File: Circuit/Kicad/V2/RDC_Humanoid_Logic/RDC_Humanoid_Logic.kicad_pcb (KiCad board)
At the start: 2 copper layers, 157 x 137 mm, 70 parts, among them J1 XT30, J2 Conn_01x03, J3 Conn_01x03, J4 Raspi_connect, Q1 Q_PMOS_GDS, Q2 Q_PMOS_GDS, SW1 SW_SPDT, SW2 SW_SPDT, SW3 SW_SPDT, U1 ISOW1044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

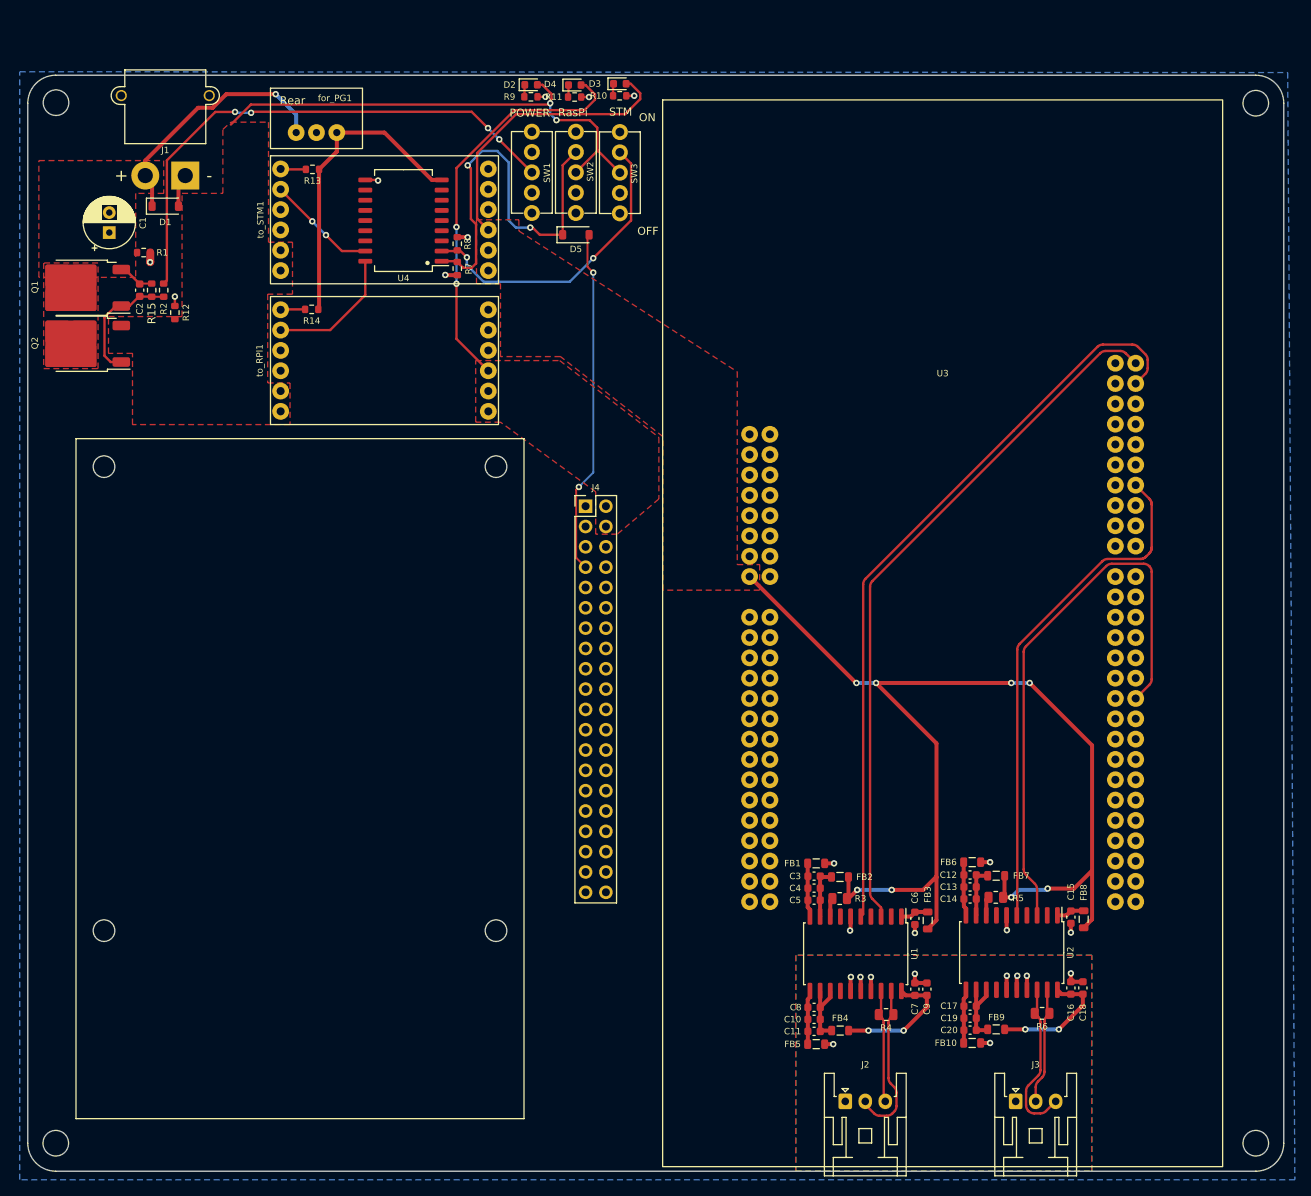
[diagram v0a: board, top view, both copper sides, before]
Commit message: V2をUpdate。FrontをベタGND、CANトランシーバのSTANDBYとINをGNDに接続、ビアを複数配置、XT30->XT60に更新、D1を回路図通りショットキーバリアダイオードに変更した。
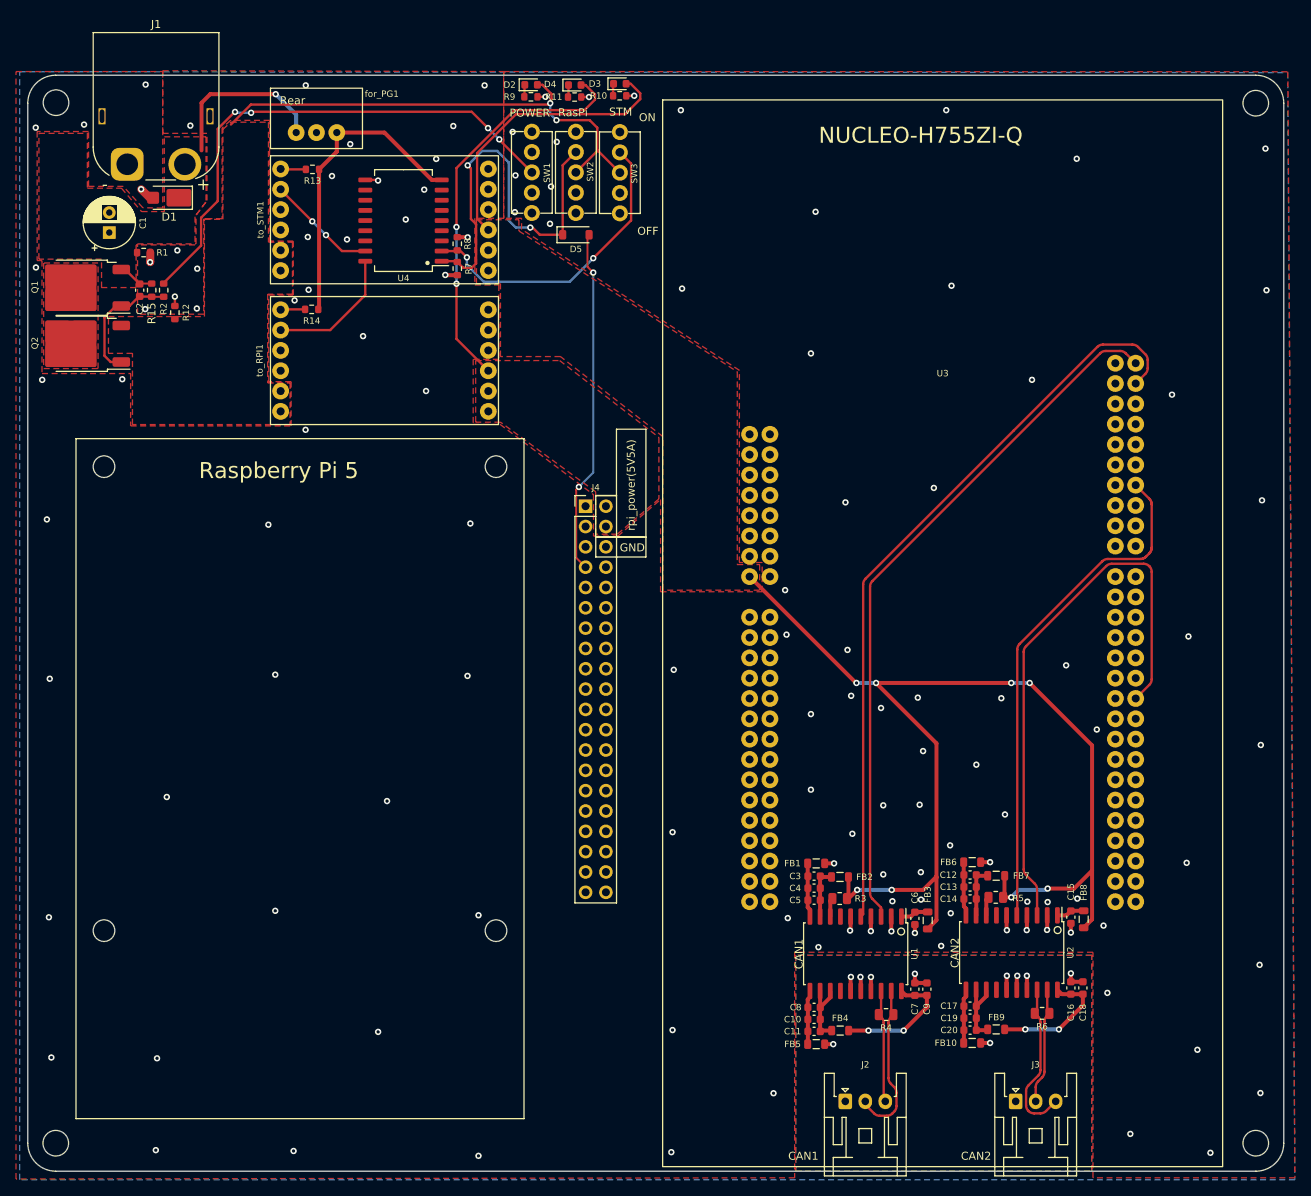
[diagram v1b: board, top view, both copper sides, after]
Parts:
- D1: value D -> D_Schottky; footprint Diode_SMD:D_SOD-123 -> Diode_SMD:Vishay_SMPA
- J1: value XT30 -> XT60; footprint Connector_AMASS:AMASS_XT30PW-M_1x02_P2.50mm_Horizontal -> Connector_AMASS:AMASS_XT60PW-M_1x02_P7.20mm_Horizontal
- moved J1 7.39 mm to (79.9, 35.5)
- moved D1 1.16 mm to (85.2, 39.6), turned to 180 degrees
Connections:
- U1 pad 2: /CAN_Trans1/GPIO -> GND
- U1 pad 4: /CAN_Trans1/STANBY -> GND
- U2 pad 2: /CAN_Trans2/GPIO -> GND
- U2 pad 4: /CAN_Trans2/STANBY -> GND
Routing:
- net +12V: track 36.2 -> 26.1 mm
- net GND: track 22.2 -> 27.3 mm, vias 14 -> 126
- net Net-(SW1-B): track 67.0 -> 65.5 mm
- added copper zone on F.Cu, net GND
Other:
- board text added: "CAN1"
- board text added: "CAN2"
- board text added: "GND"
- board text added: "NUCLEO-H755ZI-Q"
- board text added: "RDC_Bipedal_Robot - Circuit Name : Logic_Board - Version : 2.0 - Update Date : 2025/03/11 - Author Name - Main : Yuya Mochizuki - Sub : Yusuke Yamasaki"
- board text added: "Raspberry Pi 5"
- board text added: "rpi_power(5V5A)"

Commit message: V2基板手直し
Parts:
- moved R12 0.10 mm to (86.0, 54.0)
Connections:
- C10 pad 2: GND3 -> Net-(U1-GND2)
- C11 pad 2: GND3 -> Net-(U1-GND2)
- C12 pad 2: GND2 -> Net-(U2-GND1)
- C13 pad 2: GND2 -> Net-(U2-GND1)
- C14 pad 2: GND2 -> Net-(U2-GND1)
- C17 pad 2: GND3 -> Net-(U2-GND2)
- C19 pad 2: GND3 -> Net-(U2-GND2)
- C20 pad 2: GND3 -> Net-(U2-GND2)
- C3 pad 2: GND2 -> Net-(U1-GND1)
- C4 pad 2: GND2 -> Net-(U1-GND1)
- C5 pad 2: GND2 -> Net-(U1-GND1)
- C8 pad 2: GND3 -> Net-(U1-GND2)
- FB1 pad 2: GND2 -> Net-(U1-GND1)
- FB10 pad 1: GND3 -> Net-(U2-GND2)
- FB5 pad 1: GND3 -> Net-(U1-GND2)
- FB6 pad 2: GND2 -> Net-(U2-GND1)
- U1 pad 10: GND2 -> Net-(U1-GND1)
- U1 pad 11: GND3 -> Net-(U1-GND2)
- U2 pad 10: GND2 -> Net-(U2-GND1)
- U2 pad 11: GND3 -> Net-(U2-GND2)
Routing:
- net GND3: track 13.6 -> 0.00 mm
- net GND2: track 13.5 -> 0.00 mm
- net Net-(U2-GND2): track 0.00 -> 6.79 mm
- net Net-(U1-GND2): track 0.00 -> 6.79 mm
- net Net-(U1-GND1): track 0.00 -> 6.77 mm
- net Net-(U2-GND1): track 0.00 -> 6.77 mm
- net GND: vias 126 -> 128
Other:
- board text added: "RDC_Bipedal_Robot - Circuit Name : Logic_Board - Version : 2.0 - Designed Date : 2025/03/11 - Designer Name - Yuya Mochizuki - Yusuke Yamasaki"
- board text removed: "RDC_Bipedal_Robot - Circuit Name : Logic_Board - Version : 2.0 - Update Date : 2025/03/11 - Author Name - Main : Yuya Mochizuki - Sub : Yusuke Yamasaki"

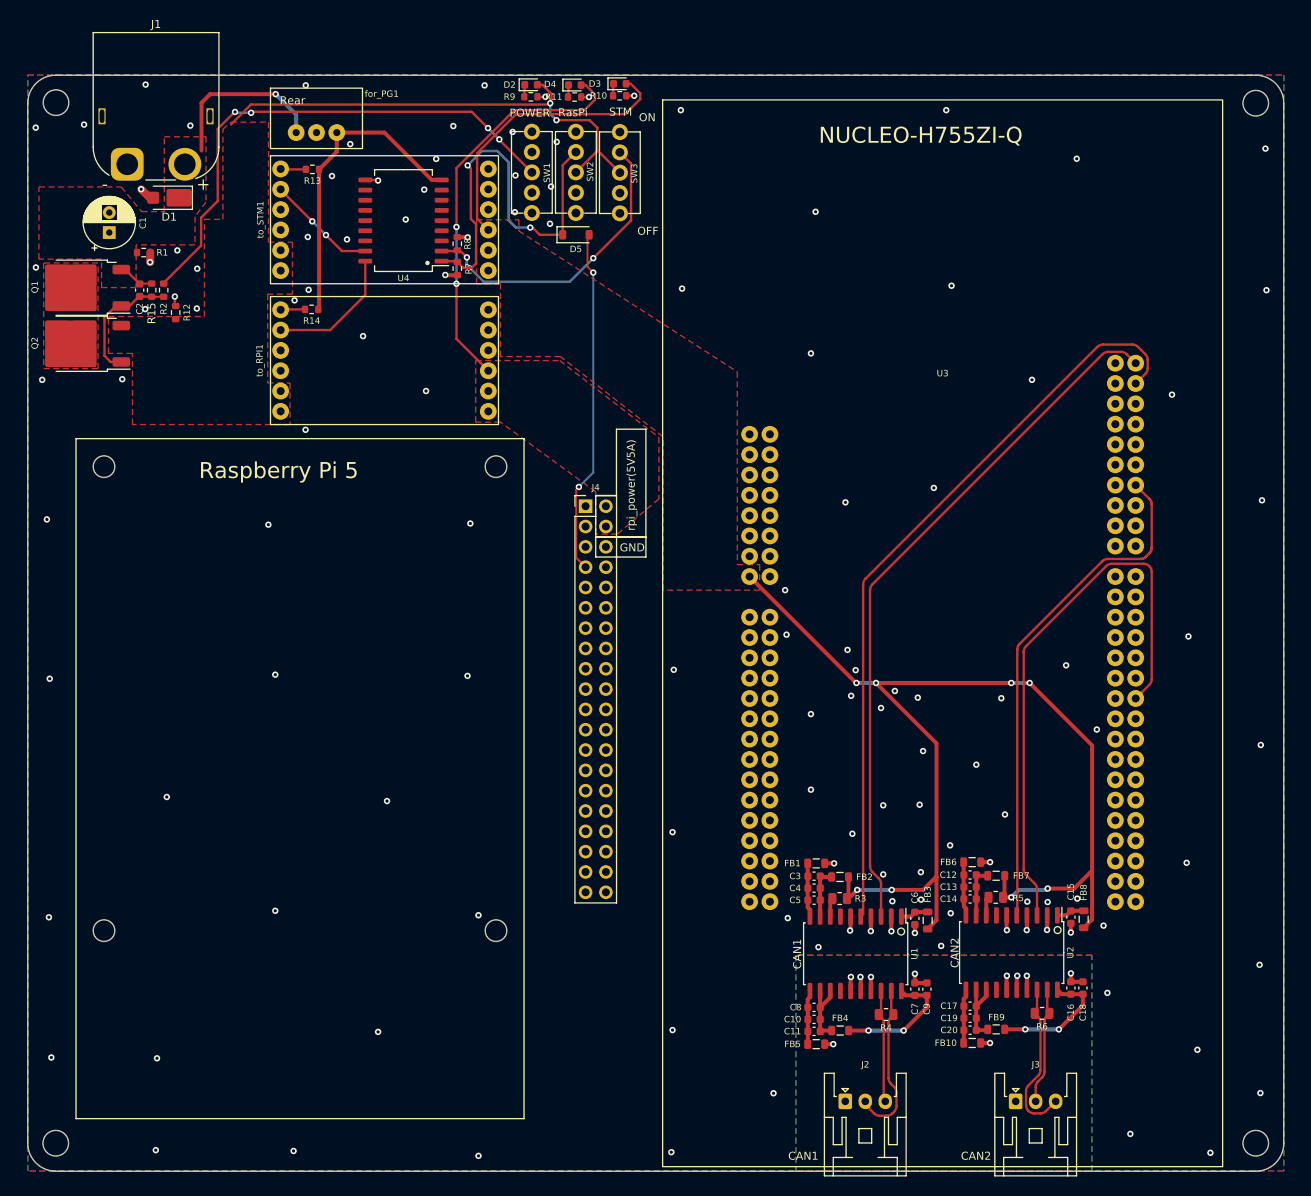
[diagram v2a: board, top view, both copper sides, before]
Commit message: ビアを増やした。おおよそV2は良いだろう
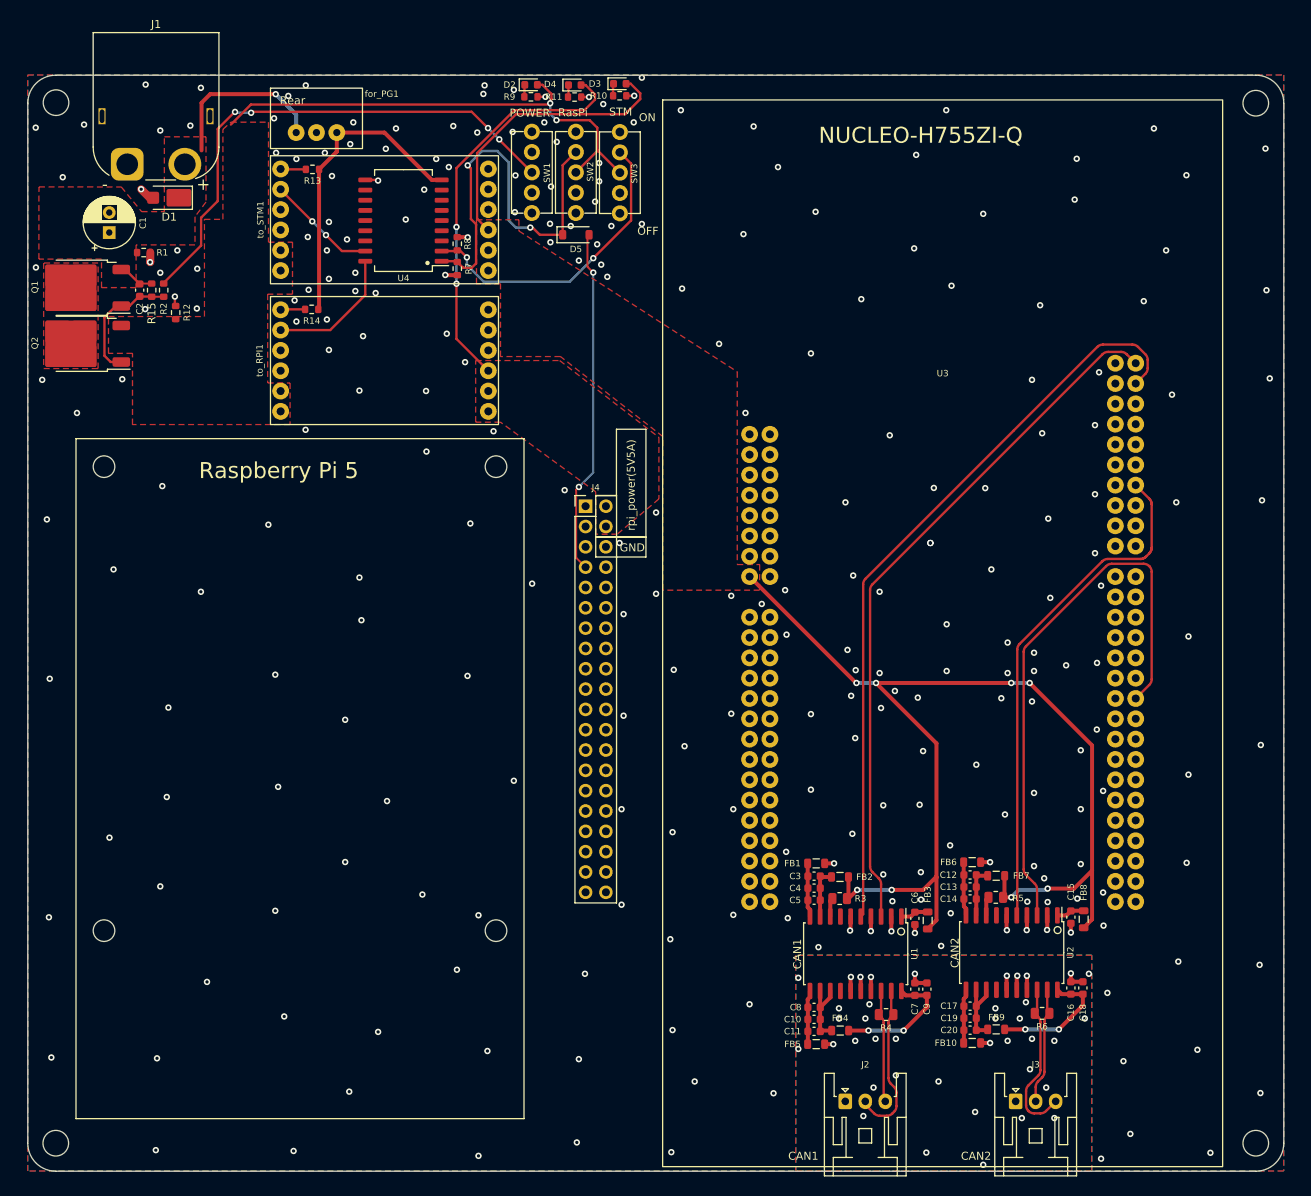
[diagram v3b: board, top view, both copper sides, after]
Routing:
- net GND1: vias 10 -> 39
- net GND: vias 128 -> 268

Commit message: 部品表の作成、多少のFootPrint、PCBの変更
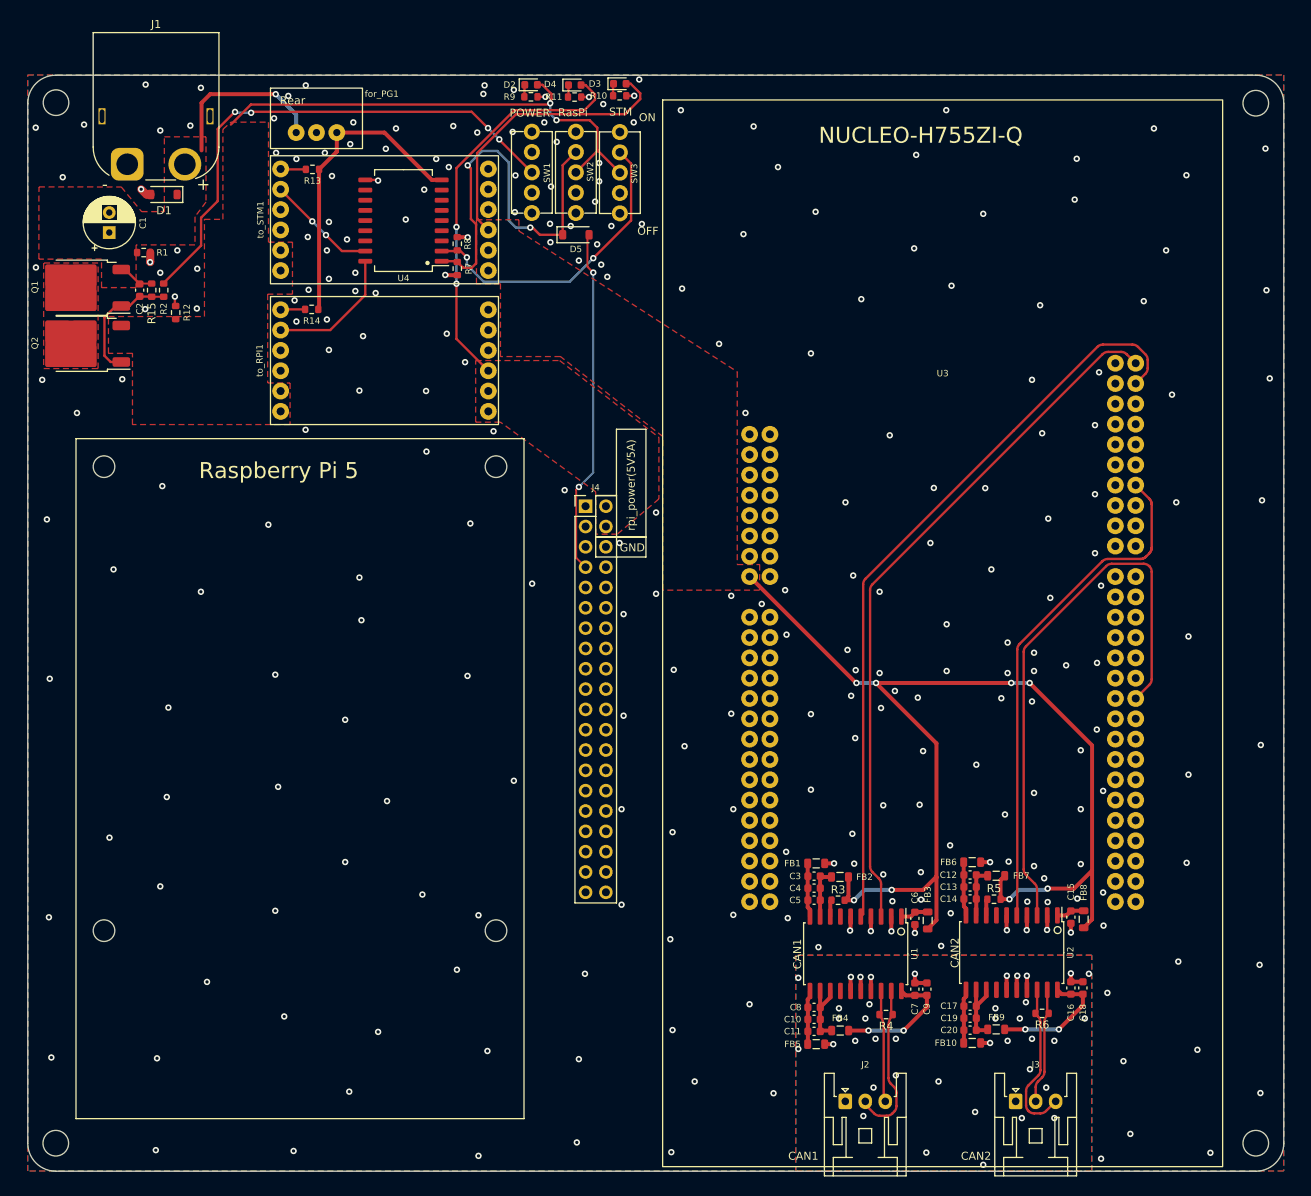
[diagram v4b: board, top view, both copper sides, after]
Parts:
- D1: footprint Diode_SMD:Vishay_SMPA -> Diode_SMD:D_SOD-123
- R3, R4, R5, R6: footprint Resistor_SMD:R_0805_2012Metric -> Resistor_SMD:R_0603_1608Metric
- moved D1 0.78 mm to (84.5, 39.2)
- moved R5 0.32 mm to (188.3, 127.3)
- moved R3 0.29 mm to (168.8, 127.5)
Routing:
- net +5V: track 175.9 -> 177.4 mm
- net GND: track 27.3 -> 26.8 mm, vias 268 -> 269
